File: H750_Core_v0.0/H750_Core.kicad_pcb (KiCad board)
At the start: 4 copper layers, 70.1 x 71.1 mm, 131 parts, among them CN1 DF9-51P-1V_LEFT, CN2 DF9-51P-1V_RIGHT, CN3 DFU_CONN, CN4 RJ45, U1 750VB_3Parts, U11 TPS786_5V, U12 TPS786_3V3, U13 TC58BVG1S3HTA00, U14 IS25LP256D, U5 ESDALC6V1W5, U7 LAN8742A-CZ-TR, U8 USBLC6-4, U9 H1102NL, X1 NX2016SA 25MHz, X2 NX3215SA 32.768KHz, X3 NX2016SA 25MHz

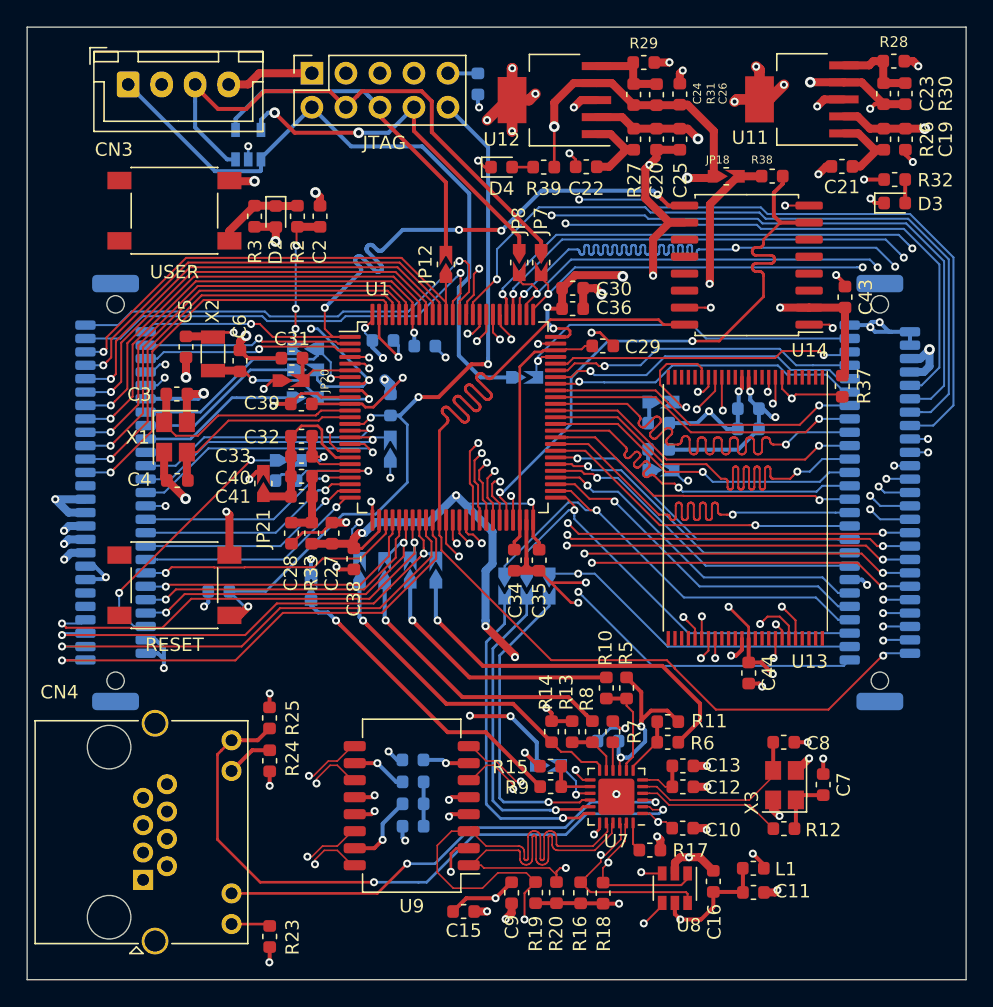
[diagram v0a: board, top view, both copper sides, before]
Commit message: 修改编程接口
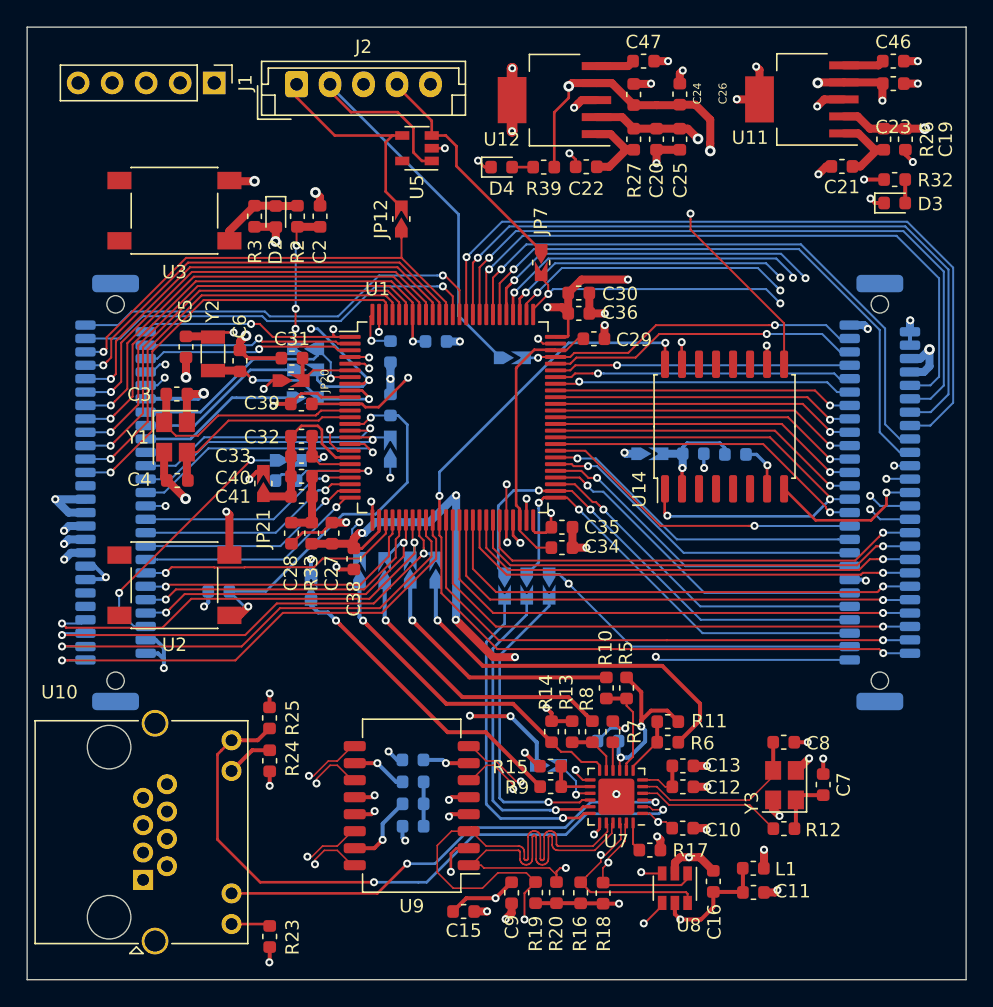
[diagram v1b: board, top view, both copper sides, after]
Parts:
- removed C42: 4.7uF, Capacitor_SMD:C_0603_1608Metric
- removed C44, C45: 100nF, Capacitor_SMD:C_0603_1608Metric
- removed JP22: Jumper_2_Open, H750_Core:JP
- removed JP23, JP8: Jumper_2_Bridged, H750_Core:JP
- removed JTAG: JTAG, Connector_PinSocket_2.54mm:PinSocket_2x05_P2.54mm_Vertical
- removed R28: 25K, Resistor_SMD:R_0603_1608Metric
- removed R29: 30.1K, Resistor_SMD:R_0603_1608Metric
- removed R30: 79K, Resistor_SMD:R_0603_1608Metric
- removed R31: 52.3K, Resistor_SMD:R_0603_1608Metric
- removed R35, R36, R37, R4: 10K, Resistor_SMD:R_0603_1608Metric
- removed U13: TC58BVG1S3HTA00, Package_SO:TSOP-I-48_18.4x12mm_P0.5mm
- added C46: 10nF, Capacitor_SMD:C_0603_1608Metric, F.Cu at (172.4, 43.2)
- added C47: 10nF, Capacitor_SMD:C_0603_1608Metric, F.Cu at (153.7, 43.2)
- added J1: DFU_CONN, Connector_PinHeader_2.54mm:PinHeader_1x05_P2.54mm_Vertical, F.Cu at (121.7, 44.8)
- C25: value 10uF -> 2.2uF
- C26: value 4.7uF -> 2.2uF
- C43, JP18, R38: moved to B.Cu
- J2: renamed from CN3; footprint Connector_JST:JST_XH_B4B-XH-A_1x04_P2.50mm_Vertical -> Connector_JST:JST_EH_B5B-EH-A_1x05_P2.50mm_Vertical
- U5: moved to F.Cu
- moved JP18 21.5 mm to (154.2, 72.5)
- moved R38 21.0 mm to (160.6, 72.5)
- moved C43 16.3 mm to (157.4, 72.5), turned to 180 degrees
- moved U5 12.6 mm to (136.8, 49.7), turned to 180 degrees
- moved J2 12.6 mm to (127.8, 44.9)
- moved U14 12.2 mm to (159.8, 70.5), turned to 90 degrees
- moved JP12 4.75 mm to (135.6, 55.0)
- moved C34 3.68 mm to (147.6, 79.5), turned to 0 degrees
- moved C35 2.99 mm to (147.6, 78.0), turned to 0 degrees
- moved JP6 1.72 mm to (143.9, 65.3)
- moved C23 1.04 mm to (172.4, 44.9), turned to 0 degrees
- moved C37 1.01 mm to (134.8, 64.9), turned to 270 degrees
- moved R1 0.91 mm to (138.2, 64.1)
- moved C29 0.85 mm to (150.0, 63.9)
- moved C36 0.58 mm to (148.9, 62.0)
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- renumbered CN4 to U10, RESET to U2, USER to U3, CN1 to U4, CN2 to U6, X1 to Y1, X2 to Y2, X3 to Y3
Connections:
- net NAND_Flash0 renamed PE10
- net NAND_Flash1 renamed PE9
- net NAND_Flash10 renamed PD11
- net NAND_Flash11 renamed PC8
- net NAND_Flash12 renamed PD4
- net NAND_Flash13 renamed PC6
- net NAND_Flash2 renamed PE8
- net NAND_Flash3 renamed PE7
- net NAND_Flash4 renamed PD1
- net NAND_Flash5 renamed PD0
- net NAND_Flash6 renamed PD15
- net NAND_Flash7 renamed PD14
- net NAND_Flash8 renamed PD5
- net NAND_Flash9 renamed PD12
- C23 pad 2: Net-(C23-Pad2) -> GND
- C24 pad 2: Net-(C24-Pad2) -> GND
- J2 pad 1: /U_Connectors/SWDIO -> /U_Connectors/SWO
- J2 pad 2: GND -> /U_Connectors/SWDIO
- J2 pad 3: /U_Connectors/SWCLK -> GND
- J2 pad 4: 3V3_VDD -> /U_Connectors/SWCLK
- U11 pad 5: Net-(C23-Pad2) -> Net-(C46-Pad1)
- U12 pad 5: Net-(C24-Pad2) -> Net-(C47-Pad1)
- U5 pad 5: /U_Connectors/T_JTDI -> Net-(U5-Pad5)
- U6 pad 16: PE11 -> PE15
- U6 pad 17: PE12 -> PE14
- U6 pad 19: PE14 -> PE12
- U6 pad 20: PE15 -> PE11
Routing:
- net GND: track 181.2 -> 133.4 mm, vias 77 -> 71
- net 3V3_VDD: track 238.7 -> 284.7 mm, vias 20 -> 19
- net 3V3_PER: track 87.3 -> 41.4 mm, vias 7 -> 2
- net PD5: track 96.0 -> 57.2 mm, vias 3 -> 1
- net PD4: track 92.4 -> 54.6 mm, vias 2 -> 1
- net PD14: track 53.1 -> 23.7 mm, vias 2 -> 1
- net /NRST: track 91.8 -> 62.5 mm, vias 6 -> 4
- net PD15: track 51.5 -> 23.5 mm, vias 2 -> 1
- net /U_Connectors/T_JTDI: track 27.8 -> 0.00 mm, vias 2 -> 0
- net PC6: track 48.3 -> 23.3 mm, vias 2 -> 1
- net PD12: track 48.8 -> 24.1 mm, vias 2 -> 1
- net PD1: track 68.1 -> 45.1 mm, vias 3 -> 1
- net PD11: track 47.1 -> 24.3 mm, vias 2 -> 1
- net PC8: track 45.2 -> 22.9 mm, vias 2 -> 1
- net PD0: track 66.7 -> 44.8 mm, vias 3 -> 1
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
